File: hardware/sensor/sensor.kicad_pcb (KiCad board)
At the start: 2 copper layers, 25.7 x 45.5 mm, 64 parts, among them P1 CONN_01X05, SW1 Reset, T2 DMP10H4D2s, U1 LMR16006, U2 OPA376AIDCK, U3 CD74HC4046, U4 CD74HC4046, U5 Atmel_SAM_D09, X1 60V, X2 UART

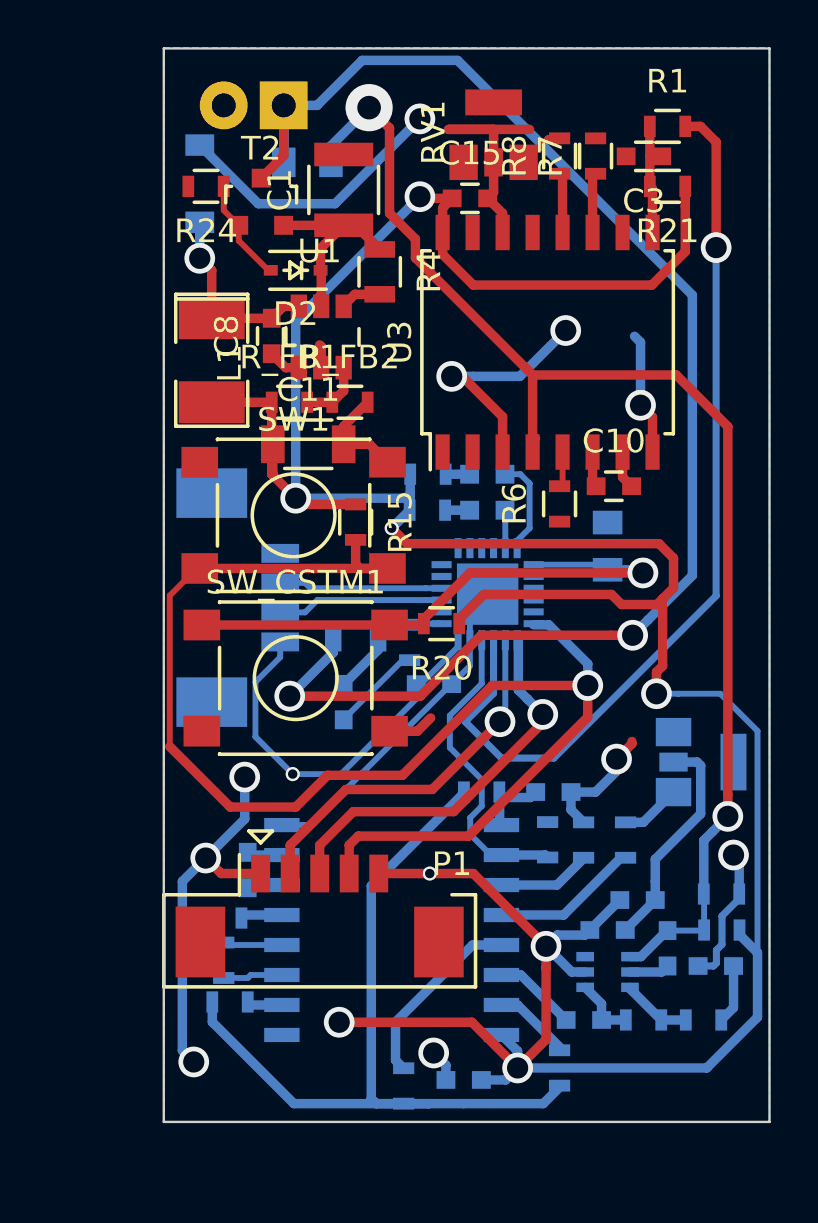
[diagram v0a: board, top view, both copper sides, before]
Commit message: PCB Bugfixes
R,C under switch removed
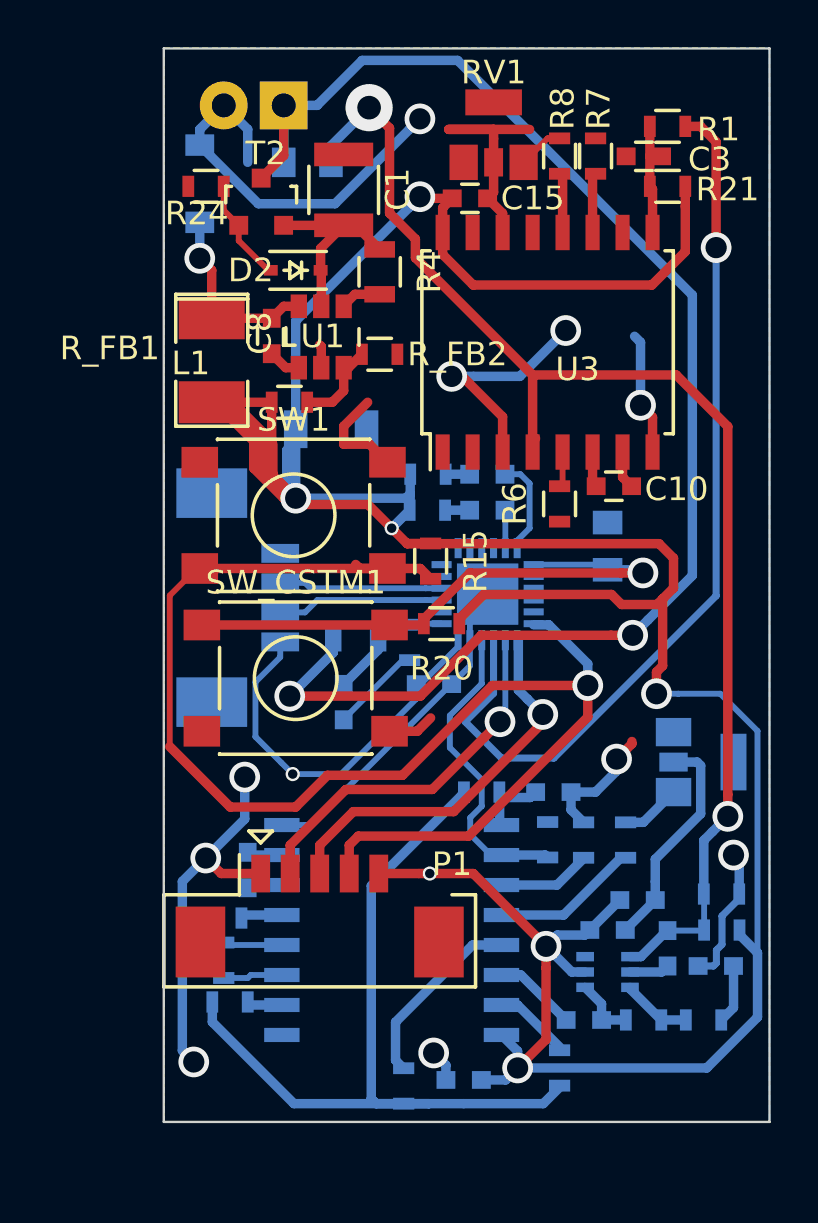
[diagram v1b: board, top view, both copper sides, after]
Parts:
- C11: moved to B.Cu
- moved R15 3.58 mm to (138.3, 75.8)
- moved R_FB2 2.39 mm to (136.1, 67.1)
- moved C11 1.16 mm to (134.1, 70.2)
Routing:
- net +3V3: track 157.8 -> 170.6 mm, vias 9 -> 8
- net GND: track 101.4 -> 106.4 mm
- net Net-(R_FB1-Pad2): track 2.73 -> 3.74 mm
- net Net-(P1-Pad4): track 58.6 -> 59.6 mm
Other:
- rule via_min_size: 0.9 -> 0.6
- board text added: "Dominik Keller"

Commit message: Gerber_Data and small fixes
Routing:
- net +3V3: track 170.6 -> 169.5 mm, vias 8 -> 7
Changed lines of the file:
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@@
   (general
     (links 137)
-    (no_connects 5)
-    (area 124.607 45.639999 153.655001 101.319)
+    (no_connects 6)
+    (area 122.153286 45.639999 153.655001 101.319)
     (thickness 1.6)
     (drawings 5)
-    (tracks 441)
+    (tracks 439)
     (zones 0)
     (modules 64)
@@
   )
   (setup
-    (last_trace_width 0.4)
+    (last_trace_width 0.25)
     (user_trace_width 0.4)
     (trace_clearance 0.2)
@@
   (segment (start 139.466 79.441) (end 137.881 81.026) (width 0.25) (layer B.Cu) (net 6))
   (segment (start 137.881 81.026) (end 137.692 81.026) (width 0.25) (layer B.Cu) (net 6))
-  (segment (start 136.652 74.422) (end 137.414 73.66) (width 0.4) (layer B.Cu) (net 6))
-  (via (at 136.652 74.422) (size 0.6) (drill 0.4) (layers F.Cu B.Cu) (net 6))
   (segment (start 152.146 95.134002) (end 152.146 92.402) (width 0.4) (layer B.Cu) (net 6))
   (segment (start 152.146 92.402) (end 151.384 91.64) (width 0.4) (layer B.Cu) (net 6))

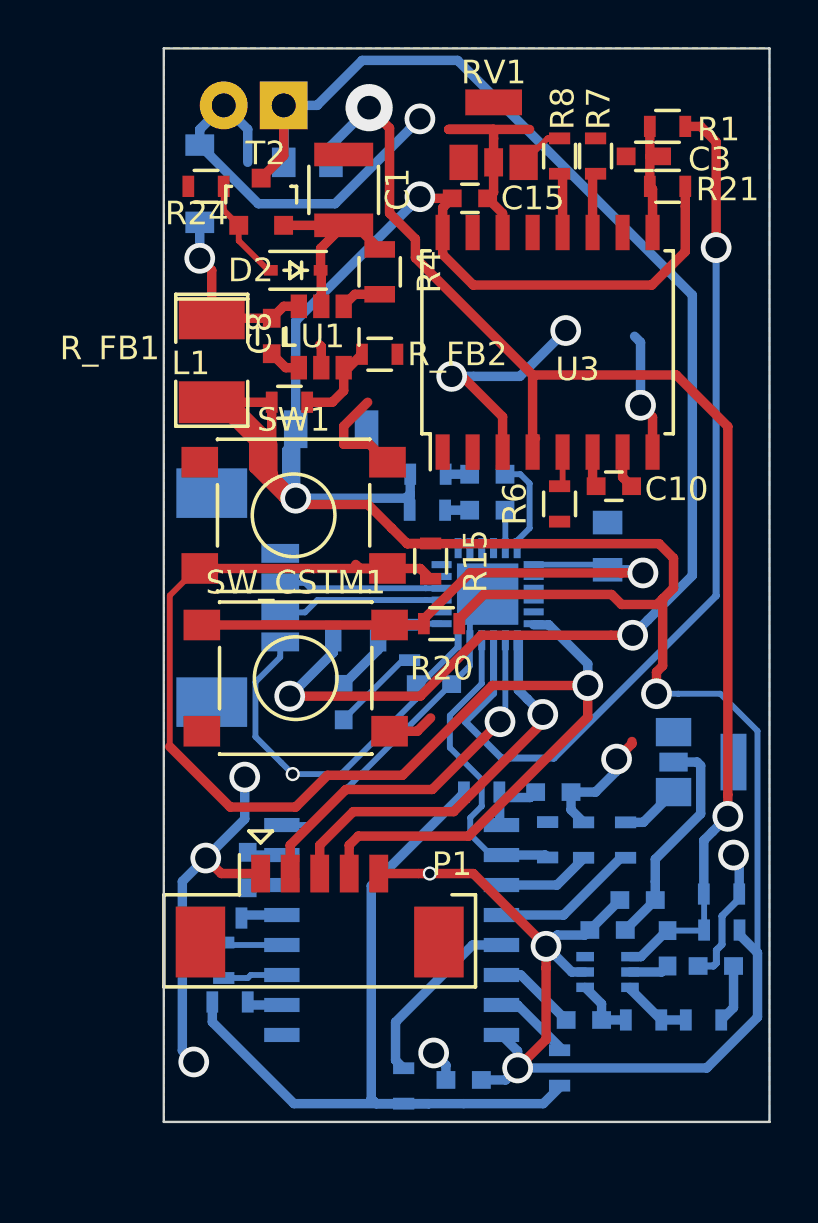
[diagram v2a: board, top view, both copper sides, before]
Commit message: Print troubleshooting
+newest Gerberfiles
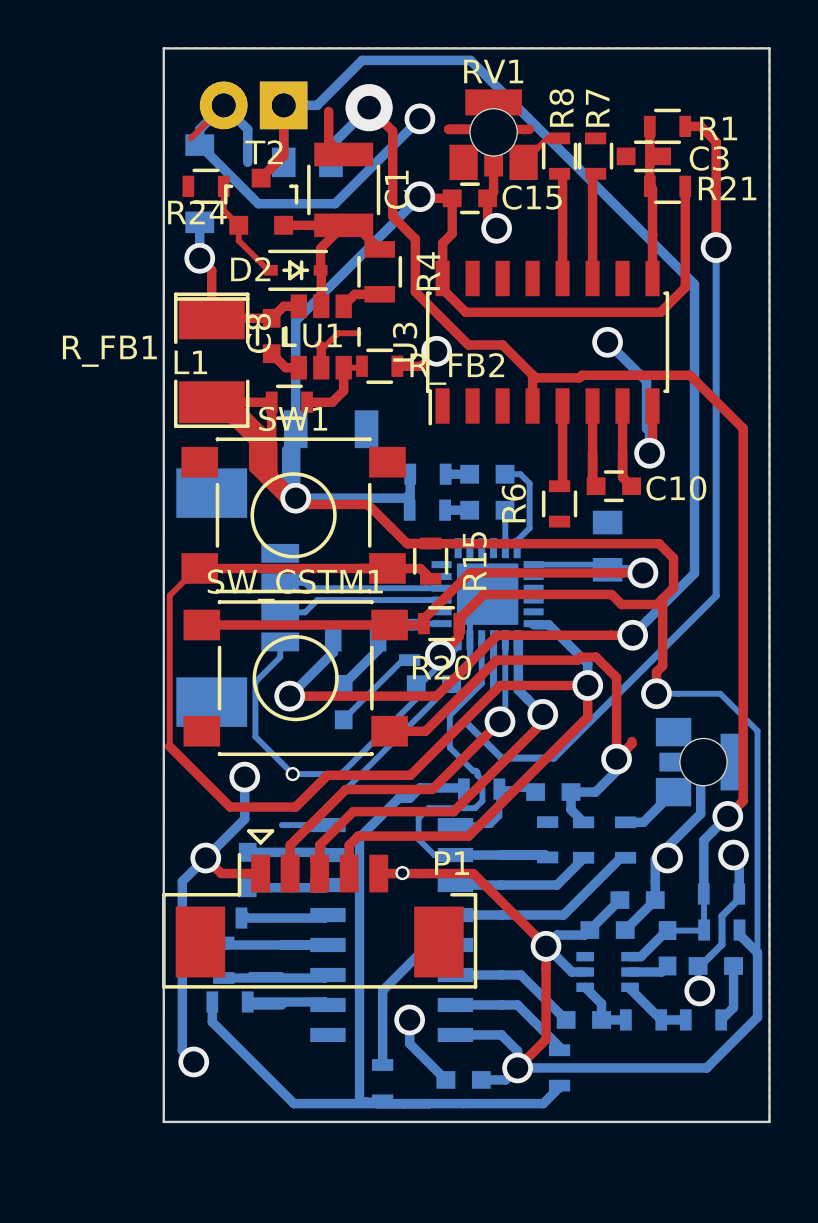
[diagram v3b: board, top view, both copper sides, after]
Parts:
- RV1, RV2: footprint pro4:EVM-1USX30B14 -> pro4:EVM-1USX30B14_poti
- U3, U4: footprint Housings_SOIC:SOIC-16_7.5x10.3mm_Pitch1.27mm -> Housings_SOIC:SOIC-16_3.9x9.9mm_Pitch1.27mm
- moved JP3.2 0.90 mm to (136.3, 97.9)
- moved R_FB2 0.51 mm to (136.1, 67.6)
- moved R9 0.13 mm to (140.5, 85.5)
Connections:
- P1 pad : GND -> (no net)
- X2 pad : GND -> (no net)
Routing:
- net GND: track 106.4 -> 119.8 mm, vias 10 -> 13
- net +3V3: track 169.5 -> 177.2 mm, vias 7 -> 8
- net /RX1_out: track 13.2 -> 20.0 mm
- net Net-(JP3.4-Pad1): track 2.50 -> 8.76 mm
- net /JP2: track 2.51 -> 6.98 mm
- net Net-(JP3.1-Pad1): track 1.50 -> 4.95 mm
- net Net-(R6-Pad2): track 1.50 -> 4.77 mm
- net Net-(C10-Pad1): track 1.51 -> 4.75 mm
- net Net-(C10-Pad2): track 1.60 -> 4.62 mm
- net /VCOin: track 34.5 -> 37.0 mm
- net Net-(C3-Pad1): track 4.69 -> 7.13 mm
- net Net-(C13-Pad2): track 1.49 -> 3.63 mm
- net Net-(R11-Pad2): track 1.76 -> 3.89 mm
- net Net-(C13-Pad1): track 1.49 -> 3.61 mm
- net Net-(R8-Pad1): track 2.54 -> 4.49 mm
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
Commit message: PCB V3 and schematic updated
s: added FET
PCB: ASK added DRC still outstanding
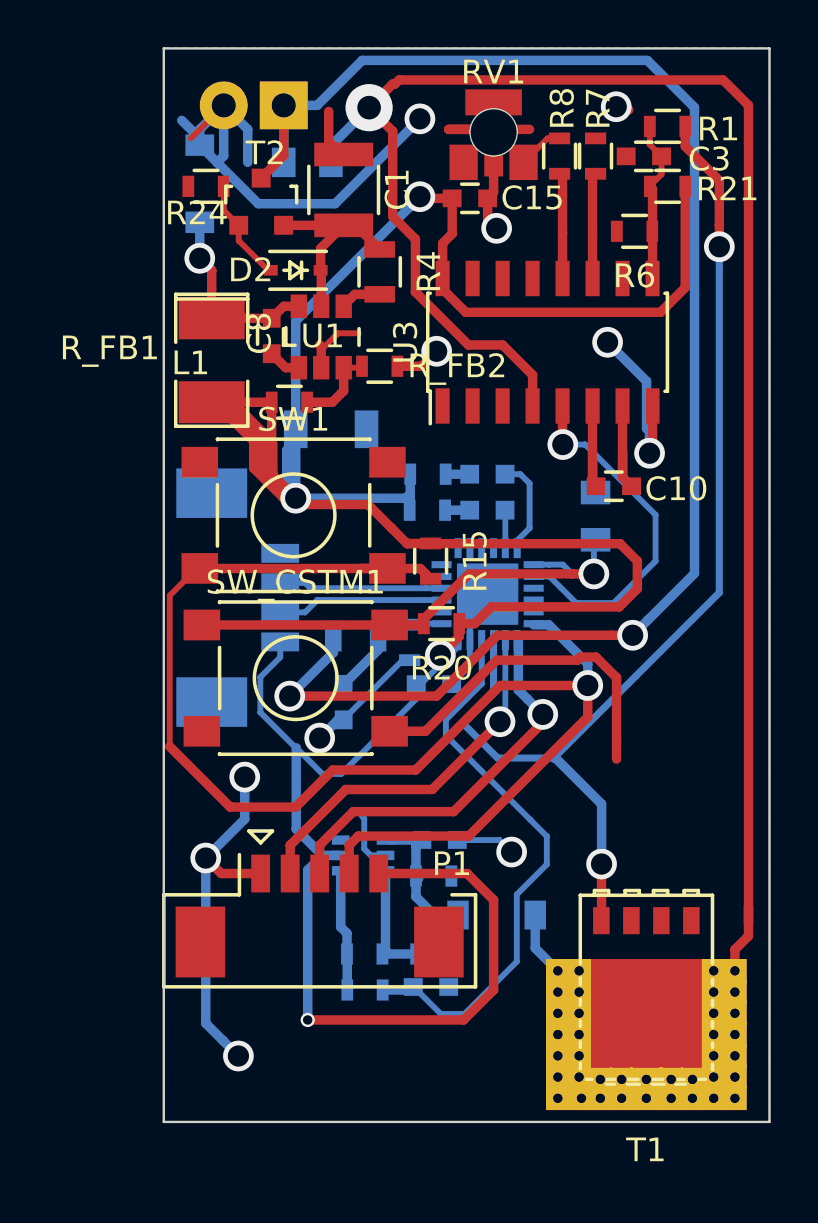
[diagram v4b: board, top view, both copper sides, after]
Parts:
- removed C13, C2, C7, C9: C_Small, Capacitors_SMD:C_0603
- removed C16: 100n, Capacitors_SMD:C_0603
- removed C6: 1u, Capacitors_SMD:C_0603
- removed JP3.1, JP3.2, JP3.3, JP3.4, R12, R13, R9: R_Small, Resistors_SMD:R_0603
- removed R11: 10k, Resistors_SMD:R_0603
- removed R14: 50k, Resistors_SMD:R_0603
- removed RV2: POT, pro4:EVM-1USX30B14_poti
- removed U4: CD74HC4046, Housings_SOIC:SOIC-16_3.9x9.9mm_Pitch1.27mm
- added D3: D_Schottky_Small, Diodes_SMD:SOD-123, B.Cu at (141.1, 90.8)
- added T1: BUK9Y22, TO_SOT_Packages_SMD:SOT-669_LFPAK_ThermalVias-1, F.Cu at (147.4, 93.9)
- R6: value 10k -> x
- moved R3 15.3 mm to (135.5, 92.5)
- moved R5 13.0 mm to (138.4, 89.2)
- moved R2 12.2 mm to (138.4, 92.5), turned to 0 degrees
- moved C4 12.1 mm to (138.3, 93.9), turned to 0 degrees
- moved R6 12.0 mm to (146.9, 61.8), turned to 180 degrees
- moved R10 11.9 mm to (135.5, 94.0), turned to 180 degrees
- moved U2 11.5 mm to (135.4, 88.3)
- moved C5 8.76 mm to (138.7, 87.6)
- moved C17 1.37 mm to (145.3, 73.9)
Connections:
- C4 pad 1: Net-(C4-Pad1) -> /RX1_out
- C5 pad 1: +3V3 -> Net-(C5-Pad1)
- R10 pad 1: Net-(C9-Pad2) -> /RX1_out
- R2 pad 1: +3V3 -> Net-(R2-Pad1)
- R2 pad 2: /coupling -> GND
- R3 pad 1: /coupling -> Net-(R10-Pad2)
- R3 pad 2: GND -> Net-(R2-Pad1)
- R5 pad 1: Net-(C4-Pad1) -> GND
- R5 pad 2: Net-(R10-Pad2) -> Net-(C5-Pad1)
- R6 pad 1: GND -> Net-(C3-Pad1)
- R6 pad 2: Net-(R6-Pad2) -> GND
- RV1 pad 1: Net-(RV1-Pad1) -> (no net)
- U2 pad 1: /coupling -> Net-(C5-Pad1)
- U2 pad 3: Net-(R10-Pad2) -> Net-(R2-Pad1)
- U2 pad 4: Net-(C9-Pad2) -> Net-(R10-Pad2)
- U3 pad 1: Net-(U3-Pad1) -> (no net)
- U3 pad 10: Net-(U3-Pad10) -> (no net)
- U3 pad 13: Net-(U3-Pad13) -> (no net)
- U3 pad 15: Net-(U3-Pad15) -> (no net)
- U3 pad 2: Net-(U3-Pad2) -> (no net)
- U3 pad 5: Net-(R6-Pad2) -> /INH-Tx
- U5 pad 10: Net-(U5-Pad10) -> (no net)
- U5 pad 14: Net-(U5-Pad14) -> /INH-Tx
- U5 pad 15: Net-(U5-Pad15) -> (no net)
- U5 pad 16: Net-(U5-Pad16) -> (no net)
- U5 pad 17: Net-(U5-Pad17) -> (no net)
- U5 pad 2: Net-(U5-Pad2) -> (no net)
- U5 pad 5: Net-(U5-Pad5) -> (no net)
- U5 pad 6: Net-(U5-Pad6) -> (no net)
- U5 pad 7: Net-(U5-Pad7) -> (no net)
- U5 pad 8: Net-(U5-Pad8) -> (no net)
- U5 pad 9: Net-(U5-Pad9) -> (no net)
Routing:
- net /VCOin: track 37.0 -> 0.00 mm
- net +3V3: track 177.2 -> 143.5 mm, vias 8 -> 4
- net GND: track 119.8 -> 92.3 mm, vias 13 -> 11
- net /coupling: track 55.0 -> 76.7 mm, vias 2 -> 1
- net /INH-Tx: track 0.00 -> 15.1 mm, vias 0 -> 1
- net Net-(JP3.4-Pad1): track 8.76 -> 0.00 mm
- net Net-(R13-Pad1): track 8.21 -> 0.00 mm
- net /TX1_in: track 38.9 -> 46.5 mm, vias 1 -> 2
- net Net-(JP3.2-Pad2): track 7.03 -> 0.00 mm
- net /JP2: track 6.98 -> 0.00 mm
- net Net-(C5-Pad1): track 0.00 -> 6.18 mm
- net Net-(R12-Pad1): track 5.92 -> 0.00 mm
- net Net-(C9-Pad1): track 5.44 -> 0.00 mm
- net Net-(JP3.3-Pad2): track 5.19 -> 0.00 mm
- net Net-(R2-Pad1): track 0.00 -> 5.01 mm
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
